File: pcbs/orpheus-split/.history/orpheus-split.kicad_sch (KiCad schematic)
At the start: 43 parts, among them SW1 SW_Push, SW10 SW_Push, SW11 SW_Push, SW12 SW_Push, SW13 SW_Push, SW14 SW_Push, SW15 SW_Push, SW16 SW_Push, SW17 SW_Push, SW18 SW_Push, SW19 SW_Push, SW2 SW_Push, SW20 SW_Push, SW21 SW_Push, SW3 SW_Push, SW4 SW_Push, SW5 SW_Push, SW6 SW_Push, SW7 SW_Push, SW8 SW_Push, SW9 SW_Push

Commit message: working on the pcb
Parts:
- SW1, SW10, SW11, SW12, SW13, SW14, SW15, SW16, SW17, SW18, SW19, SW2, SW20, SW21, SW3, SW4, SW5, SW6, SW7, SW8, SW9: footprint (none) -> PCM_Switch_Keyboard_Hotswap_Kailh:SW_Hotswap_Kailh_Choc_V1
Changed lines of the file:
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@@
 			)
 		)
-		(property "Footprint" ""
+		(property "Footprint" "PCM_Switch_Keyboard_Hotswap_Kailh:SW_Hotswap_Kailh_Choc_V1"
 			(at 97.79 76.2 0)
 			(hide yes)
@@
 			)
 		)
-		(property "Footprint" ""
+		(property "Footprint" "PCM_Switch_Keyboard_Hotswap_Kailh:SW_Hotswap_Kailh_Choc_V1"
 			(at 62.23 59.69 0)
 			(hide yes)
@@
 			)
 		)
-		(property "Footprint" ""
+		(property "Footprint" "PCM_Switch_Keyboard_Hotswap_Kailh:SW_Hotswap_Kailh_Choc_V1"
 			(at 97.79 59.69 0)
 			(hide yes)
@@
 			)
 		)
-		(property "Footprint" ""
+		(property "Footprint" "PCM_Switch_Keyboard_Hotswap_Kailh:SW_Hotswap_Kailh_Choc_V1"
 			(at 97.79 48.26 0)
 			(hide yes)
@@
 			)
 		)
-		(property "Footprint" ""
+		(property "Footprint" "PCM_Switch_Keyboard_Hotswap_Kailh:SW_Hotswap_Kailh_Choc_V1"
 			(at 44.45 59.69 0)
 			(hide yes)
@@
 			)
 		)
-		(property "Footprint" ""
+		(property "Footprint" "PCM_Switch_Keyboard_Hotswap_Kailh:SW_Hotswap_Kailh_Choc_V1"
 			(at 26.67 48.26 0)
 			(hide yes)
@@
 			)
 		)
-		(property "Footprint" ""
+		(property "Footprint" "PCM_Switch_Keyboard_Hotswap_Kailh:SW_Hotswap_Kailh_Choc_V1"
 			(at 44.45 35.56 0)
 			(hide yes)
@@
 			)
 		)
-		(property "Footprint" ""
+		(property "Footprint" "PCM_Switch_Keyboard_Hotswap_Kailh:SW_Hotswap_Kailh_Choc_V1"
 			(at 115.57 59.69 0)
 			(hide yes)
@@
 			)
 		)
-		(property "Footprint" ""
+		(property "Footprint" "PCM_Switch_Keyboard_Hotswap_Kailh:SW_Hotswap_Kailh_Choc_V1"
 			(at 115.57 48.26 0)
 			(hide yes)
@@
 			)
 		)
-		(property "Footprint" ""
+		(property "Footprint" "PCM_Switch_Keyboard_Hotswap_Kailh:SW_Hotswap_Kailh_Choc_V1"
 			(at 26.67 35.56 0)
 			(hide yes)
@@
 			)
 		)
-		(property "Footprint" ""
+		(property "Footprint" "PCM_Switch_Keyboard_Hotswap_Kailh:SW_Hotswap_Kailh_Choc_V1"
 			(at 115.57 76.2 0)
 			(hide yes)
@@
 			)
 		)
-		(property "Footprint" ""
+		(property "Footprint" "PCM_Switch_Keyboard_Hotswap_Kailh:SW_Hotswap_Kailh_Choc_V1"
 			(at 80.01 59.69 0)
 			(hide yes)
@@
 			)
 		)
-		(property "Footprint" ""
+		(property "Footprint" "PCM_Switch_Keyboard_Hotswap_Kailh:SW_Hotswap_Kailh_Choc_V1"
 			(at 62.23 35.56 0)
 			(hide yes)
@@
 			)
 		)
-		(property "Footprint" ""
+		(property "Footprint" "PCM_Switch_Keyboard_Hotswap_Kailh:SW_Hotswap_Kailh_Choc_V1"
 			(at 62.23 48.26 0)
 			(hide yes)
@@
 			)
 		)
-		(property "Footprint" ""
+		(property "Footprint" "PCM_Switch_Keyboard_Hotswap_Kailh:SW_Hotswap_Kailh_Choc_V1"
 			(at 80.01 35.56 0)
 			(hide yes)
@@
 			)
 		)
-		(property "Footprint" ""
+		(property "Footprint" "PCM_Switch_Keyboard_Hotswap_Kailh:SW_Hotswap_Kailh_Choc_V1"
 			(at 44.45 48.26 0)
 			(hide yes)
@@
 			)
 		)
-		(property "Footprint" ""
+		(property "Footprint" "PCM_Switch_Keyboard_Hotswap_Kailh:SW_Hotswap_Kailh_Choc_V1"
 			(at 97.79 35.56 0)
 			(hide yes)
@@
 			)
 		)
-		(property "Footprint" ""
+		(property "Footprint" "PCM_Switch_Keyboard_Hotswap_Kailh:SW_Hotswap_Kailh_Choc_V1"
 			(at 80.01 48.26 0)
 			(hide yes)
@@
 			)
 		)
-		(property "Footprint" ""
+		(property "Footprint" "PCM_Switch_Keyboard_Hotswap_Kailh:SW_Hotswap_Kailh_Choc_V1"
 			(at 80.01 76.2 0)
 			(hide yes)
@@
 			)
 		)
-		(property "Footprint" ""
+		(property "Footprint" "PCM_Switch_Keyboard_Hotswap_Kailh:SW_Hotswap_Kailh_Choc_V1"
 			(at 115.57 35.56 0)
 			(hide yes)
@@
 			)
 		)
-		(property "Footprint" ""
+		(property "Footprint" "PCM_Switch_Keyboard_Hotswap_Kailh:SW_Hotswap_Kailh_Choc_V1"
 			(at 26.67 59.69 0)
 			(hide yes)

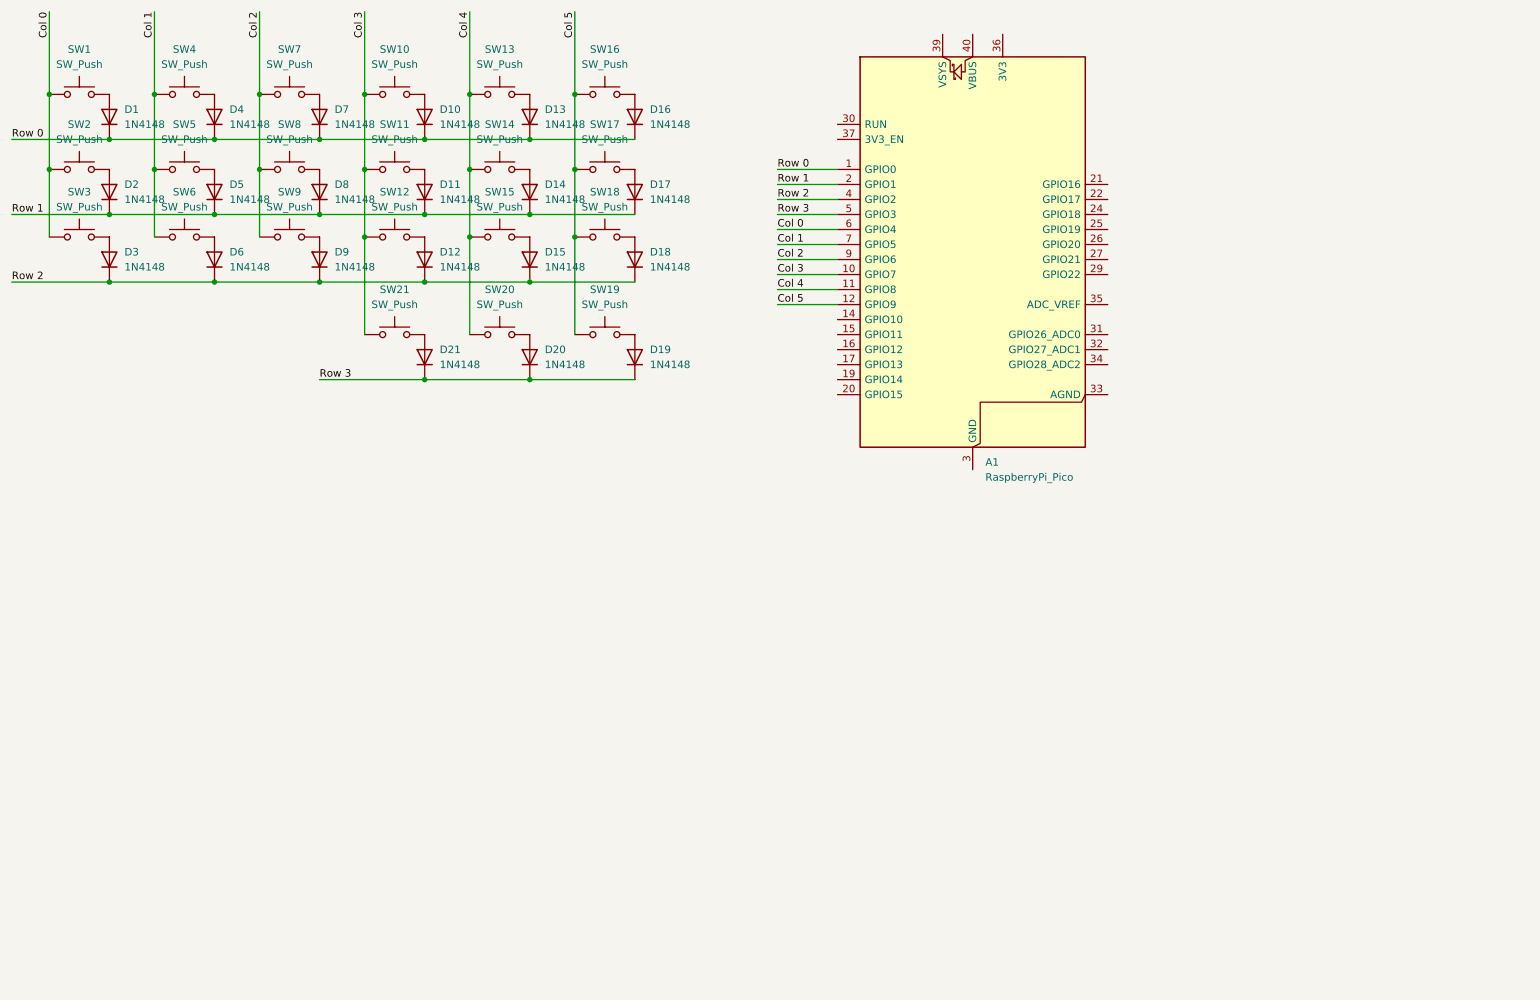
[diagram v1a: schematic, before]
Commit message: finished the left pcb
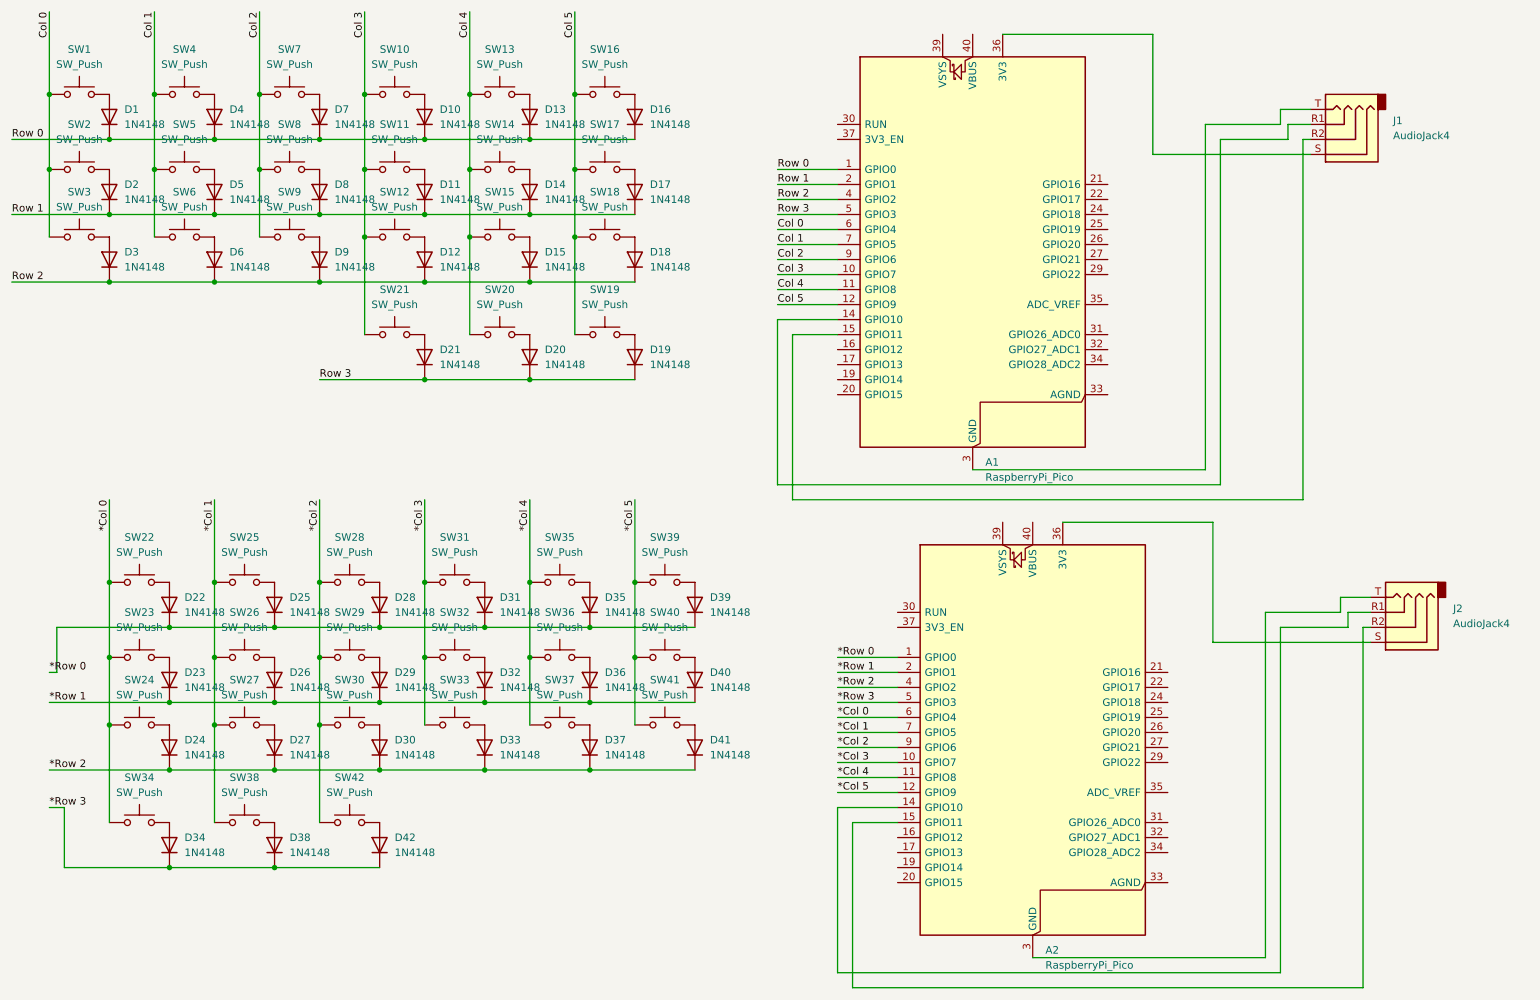
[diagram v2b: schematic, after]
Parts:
- added A2: RaspberryPi_Pico, Module:RaspberryPi_Pico_Common_Unspecified, symbol MCU_Module:RaspberryPi_Pico
- added D22, D23, D24, D25, D26, D27, D28, D29, D30, D31, D32, D33, D34, D35, D36, D37, D38, D39, D40, D41, D42: 1N4148, Diode_THT:D_DO-35_SOD27_P7.62mm_Horizontal, symbol Diode:1N4148
- added J1, J2: AudioJack4, Connector_Audio:Jack_3.5mm_PJ320D_Horizontal, symbol Connector_Audio:AudioJack4
- added SW22, SW23, SW24, SW25, SW26, SW27, SW28, SW29, SW30, SW31, SW32, SW33, SW34, SW35, SW36, SW37, SW38, SW39, SW40, SW41, SW42: SW_Push, PCM_Switch_Keyboard_Hotswap_Kailh:SW_Hotswap_Kailh_Choc_V1, symbol Switch:SW_Push
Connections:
- net at A1.13 (GND), A1.18 (GND), A1.23 (GND)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: now also J1.T
- net at A1.14 (GPIO10): now also J1.R1
- net at A1.15 (GPIO11): now also J1.R2
- net at A1.36 (3V3): now also J1.S
- new net: D37.2 (A), SW37.2
- new net: D32.2 (A), SW32.2
- new net: D30.2 (A), SW30.2
- new net: D25.2 (A), SW25.2
- new net: D22.2 (A), SW22.2
- new net: D24.2 (A), SW24.2
- new net: D23.2 (A), SW23.2
- new net: D42.2 (A), SW42.2
- new net: D26.2 (A), SW26.2
- new net: D34.2 (A), SW34.2
- new net: D40.2 (A), SW40.2
- new net: A2.14 (GPIO10), J2.R1
- new net: A2.15 (GPIO11), J2.R2
- new net: A2.36 (3V3), J2.S
- new net: A2.13 (GND), A2.18 (GND), A2.23 (GND), A2.28 (GND), A2.3 (GND), A2.38 (GND), A2.8 (GND), J2.T
- new net: D28.2 (A), SW28.2
- new net: D29.2 (A), SW29.2
- new net: D31.2 (A), SW31.2
- new net: D39.2 (A), SW39.2
- new net: D33.2 (A), SW33.2
- new net: D35.2 (A), SW35.2
- new net: D27.2 (A), SW27.2
- new net: D41.2 (A), SW41.2
- new net: D38.2 (A), SW38.2
- new net: D36.2 (A), SW36.2
- new net *Col 0: A2.6 (GPIO4), SW22.1, SW23.1, SW24.1, SW34.1
- new net *Col 1: A2.7 (GPIO5), SW25.1, SW26.1, SW27.1, SW38.1
- new net *Col 2: A2.9 (GPIO6), SW28.1, SW29.1, SW30.1, SW42.1
- new net *Col 3: A2.10 (GPIO7), SW31.1, SW32.1, SW33.1
- new net *Col 4: A2.11 (GPIO8), SW35.1, SW36.1, SW37.1
- new net *Col 5: A2.12 (GPIO9), SW39.1, SW40.1, SW41.1
- new net *Row 0: A2.1 (GPIO0), D22.1 (K), D25.1 (K), D28.1 (K), D31.1 (K), D35.1 (K), D39.1 (K)
- new net *Row 1: A2.2 (GPIO1), D23.1 (K), D26.1 (K), D29.1 (K), D32.1 (K), D36.1 (K), D40.1 (K)
- new net *Row 2: A2.4 (GPIO2), D24.1 (K), D27.1 (K), D30.1 (K), D33.1 (K), D37.1 (K), D41.1 (K)
- new net *Row 3: A2.5 (GPIO3), D34.1 (K), D38.1 (K), D42.1 (K)
